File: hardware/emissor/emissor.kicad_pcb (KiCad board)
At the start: 2 copper layers, 100 x 76 mm, 49 parts, among them J1 I2C, J2 USB-C, J3 5V EXT, J4 BOIAS, SW1 RESET, SW2 BOOT, U1 ESP32-C3-MINI-1-H4X, U2 E220-900T30D, U4 USBLC6-2SC6, U5 AP2112K-3.3

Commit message: feat(hw): layout compacto de 86x52 mm nas duas placas
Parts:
- removed H3, H4: MountingHole_3.2mm_M3, MountingHole:MountingHole_3.2mm_M3
- moved R11 73.0 mm to (80.2, 27.8)
- moved F1 51.6 mm to (75.6, 28.2)
- moved J2 48.7 mm to (14.0, 47.8), turned to 0 degrees
- moved H2 46.5 mm to (82.5, 48.5)
- moved H1 44.5 mm to (3.50, 48.5)
- moved D3 41.4 mm to (68.9, 28.8)
- moved R12 38.3 mm to (45.5, 37.7)
- moved R16 37.3 mm to (61.4, 37.7)
- moved R15 37.1 mm to (57.6, 37.7)
- moved D6 37.0 mm to (53.6, 37.9)
- moved D5 36.8 mm to (49.5, 37.9)
- moved R6 34.0 mm to (30.6, 4.12)
- moved R5 33.9 mm to (26.7, 4.12)
- moved R4 33.8 mm to (22.9, 4.12)
- moved R3 33.6 mm to (19.0, 4.12)
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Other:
- board size 100 x 76 mm -> 86 x 52 mm
- board text added: "ABERTO=RESERV."
- board text added: "EMISSOR"
- board text added: "ENTRADA 5V APENAS"
- board text added: "J3: 5V+ | GND"
- board text added: "J4: BOIA-B|GND|BOIA-A|GND"
- board text added: "JP1 PAPEL:"
- board text added: "NAO LIGAR 12V"
- board text added: "NAO LIGAR O E220"
- board text added: "SEM ANTENA!"
- board text removed: "BOIAS: BAIXA | GND | ALTA | GND"
- board text removed: "EMISSOR (RESERVATORIO)"
- board text removed: "ENTRADA 5V APENAS - NAO LIGAR 12V"
- board text removed: "JP1 PAPEL: ABERTO=RESERV."
- board text removed: "NAO LIGAR O E220 SEM ANTENA!"
- board text removed: "O E220 TRANSMITE NO BOOT"

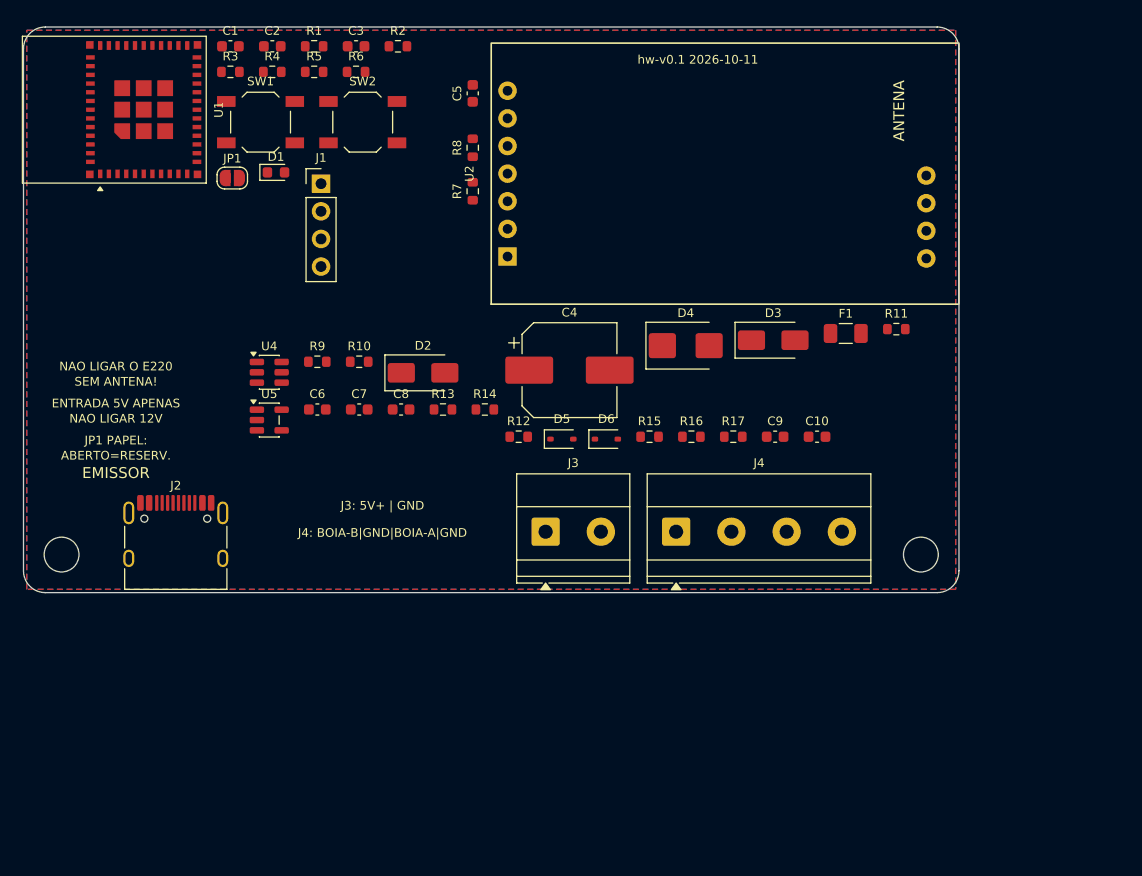
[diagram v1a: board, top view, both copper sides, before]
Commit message: wip(hw): roteador proprio, layout v2 com pecas sob o E220 (checkpoint antes de trocar para jack 12 V)
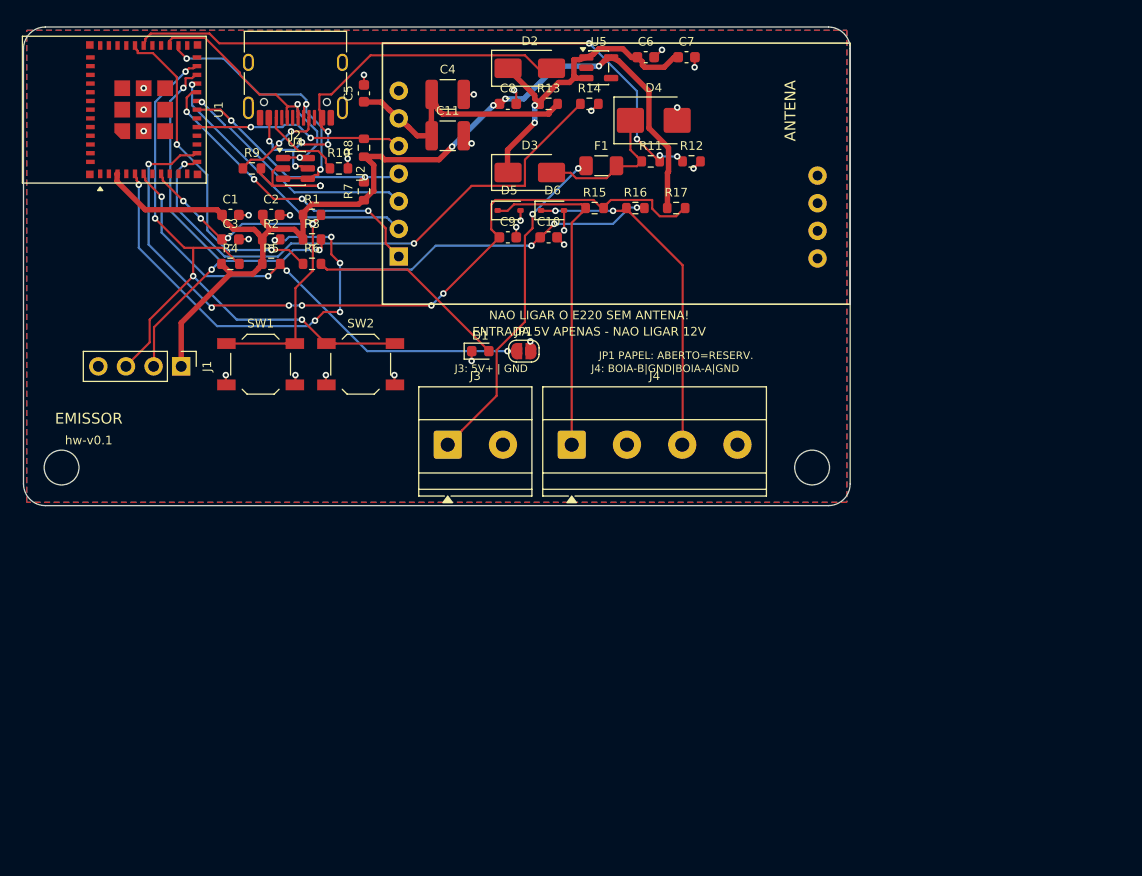
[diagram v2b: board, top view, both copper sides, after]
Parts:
- added C11: 47uF/10V, Capacitor_SMD:C_1210_3225Metric, F.Cu at (39.0, 10.0)
- C4: value 470uF/10V -> 47uF/10V; footprint Capacitor_SMD:CP_Elec_8x10.5 -> Capacitor_SMD:C_1210_3225Metric
- moved J2 44.9 mm to (25.0, 4.30), turned to 180 degrees
- moved U5 44.3 mm to (52.9, 3.75)
- moved C6 44.3 mm to (57.2, 2.77)
- moved C7 44.2 mm to (61.0, 2.77)
- moved JP1 31.2 mm to (46.0, 29.8)
- moved C10 30.7 mm to (48.3, 19.3)
- moved C9 30.7 mm to (44.5, 19.3)
- moved R12 29.9 mm to (61.4, 12.4)
- moved C8 29.8 mm to (44.5, 7.07)
- moved R13 29.7 mm to (48.3, 7.07)
- moved R14 29.7 mm to (52.0, 7.07)
- moved D2 29.7 mm to (46.5, 3.79)
- moved C4 27.7 mm to (39.0, 6.20)
- moved R11 27.3 mm to (57.7, 12.4)
- moved F1 27.3 mm to (53.1, 12.8)
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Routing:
- net +3V3: track 0.00 -> 96.5 mm, vias 0 -> 4
- net FLOAT_LOW: track 0.00 -> 73.1 mm, vias 0 -> 6
- net FLOAT_HIGH: track 0.00 -> 72.5 mm, vias 0 -> 9
- net I2C_SCL: track 0.00 -> 60.0 mm, vias 0 -> 4
- net EXT_PRESENT: track 0.00 -> 58.6 mm, vias 0 -> 4
- net BAT_ADC: track 0.00 -> 51.8 mm, vias 0 -> 2
- net ROLE_STRAP: track 0.00 -> 44.3 mm, vias 0 -> 4
- net I2C_SDA: track 0.00 -> 43.3 mm, vias 0 -> 3
- net /Alimentacao/VBUS: track 0.00 -> 40.1 mm, vias 0 -> 5
- net /MCU/MCU_EN: track 0.00 -> 36.5 mm, vias 0 -> 4
- net GND: track 0.00 -> 35.8 mm, vias 0 -> 28
- net /Entradas e Saidas/FLOAT_HIGH_IN: track 0.00 -> 31.9 mm, vias 0 -> 2
- net /Alimentacao/5V_IN: track 0.00 -> 31.2 mm, vias 0 -> 2
- net /Entradas e Saidas/FLOAT_LOW_IN: track 0.00 -> 30.8 mm
- net +5V: track 0.00 -> 30.7 mm, vias 0 -> 2
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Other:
- board size 86 x 52 mm -> 76 x 44 mm
- board text added: "ENTRADA 5V APENAS - NAO LIGAR 12V"
- board text added: "JP1 PAPEL: ABERTO=RESERV."
- board text added: "NAO LIGAR O E220 SEM ANTENA!"
- board text added: "hw-v0.1"
- board text removed: "ABERTO=RESERV."
- board text removed: "ENTRADA 5V APENAS"
- board text removed: "JP1 PAPEL:"
- board text removed: "NAO LIGAR 12V"
- board text removed: "NAO LIGAR O E220"
- board text removed: "SEM ANTENA!"
- board text removed: "hw-v0.1 2026-10-11"

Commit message: feat(hw): jack 12 V com buck AP63205, roteador proprio e serigrafia padronizada (receptor roteado; emissor com 1 net aberta)
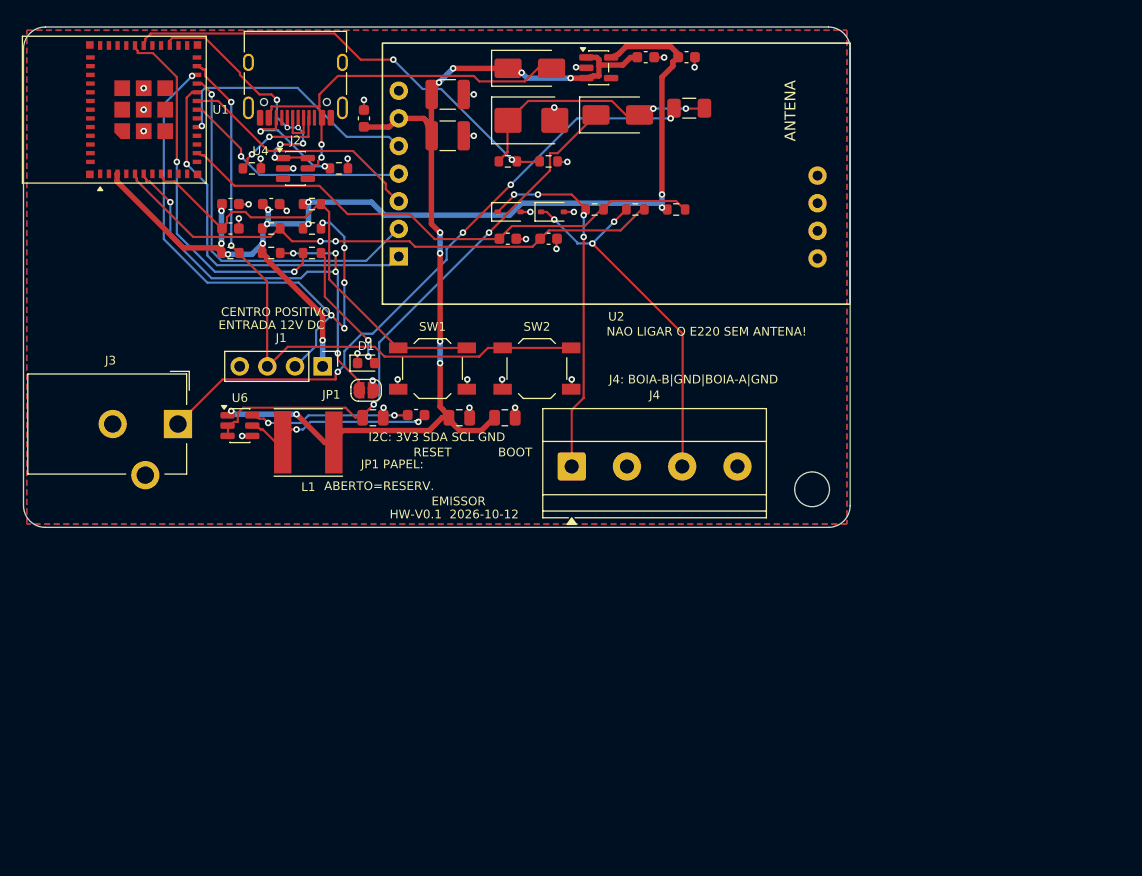
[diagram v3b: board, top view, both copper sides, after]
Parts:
- removed H2: MountingHole_3.2mm_M3, MountingHole:MountingHole_3.2mm_M3
- removed R13: 0R, Resistor_SMD:R_0603_1608Metric
- removed R14: 100k, Resistor_SMD:R_0603_1608Metric
- removed R7, R8: 10k, Resistor_SMD:R_0603_1608Metric
- added C12: 22uF/10V, Capacitor_SMD:C_0805_2012Metric, F.Cu at (40.1, 35.9)
- added C13: 22uF/10V, Capacitor_SMD:C_0805_2012Metric, F.Cu at (44.3, 35.9)
- added C14: 100nF, Capacitor_SMD:C_0603_1608Metric, F.Cu at (36.1, 35.7)
- added L1: 4.7uH, Inductor_SMD:L_Taiyo-Yuden_NR-60xx, F.Cu at (26.2, 38.2)
- added U6: AP63205WU, Package_TO_SOT_SMD:TSOT-23-6, F.Cu at (19.9, 36.6)
- C6: value 10uF -> 10uF/25V; footprint Capacitor_SMD:C_0603_1608Metric -> Capacitor_SMD:C_0805_2012Metric
- D4: value SMBJ5.0A -> SMBJ15A
- F1: value 1.5A -> 1.5A/16V
- J3: value 5V EXT -> JACK 12V; footprint TerminalBlock_Phoenix:TerminalBlock_Phoenix_MKDS-1,5-2-5.08_1x02_P5.08mm_Horizontal -> lora-pump:BarrelJack_CUI_PJ-102AH_Horizontal
- R12: value 100k -> 33k
- moved H1 69.0 mm to (72.5, 42.5)
- moved C6 41.6 mm to (32.1, 35.9)
- moved J3 24.9 mm to (14.2, 36.5), turned to -90 degrees
- moved C8 17.0 mm to (61.0, 2.77)
- moved SW2 16.2 mm to (47.2, 31.4)
- moved SW1 15.8 mm to (37.6, 31.4)
- moved JP1 14.9 mm to (31.5, 33.4)
- moved R11 13.1 mm to (44.5, 12.4)
- moved R12 13.1 mm to (48.3, 12.4)
- moved J1 13.0 mm to (27.5, 31.2)
- moved D4 11.2 mm to (46.7, 8.59)
- moved D1 10.6 mm to (31.5, 30.9)
- moved D3 9.67 mm to (54.6, 8.09)
- moved F1 9.67 mm to (61.2, 7.46)
- moved C7 3.75 mm to (57.2, 2.77)
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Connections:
- net /Alimentacao/+5V_EXT renamed /Alimentacao/+12V_F
- net /Alimentacao/5V_IN renamed /Alimentacao/12V_IN
- C11 pad 1: VCC_RF -> +5V
- C4 pad 1: VCC_RF -> +5V
- C5 pad 1: VCC_RF -> +5V
- C6 pad 1: +5V -> +12V
- D3 pad 1: +5V -> +12V
- U1 pad 12: BAT_ADC -> unconnected-(U1-IO0-Pad12)
- U2 pad 6: VCC_RF -> +5V
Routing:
- net +5V: track 30.7 -> 89.7 mm, vias 2 -> 10
- net +12V: track 0.00 -> 52.0 mm, vias 0 -> 2
- net BAT_ADC: track 51.8 -> 0.00 mm, vias 2 -> 0
- net /Alimentacao/12V_IN: track 31.2 -> 59.6 mm, vias 2 -> 4
- net VCC_RF: track 24.5 -> 0.00 mm
- net FLOAT_LOW: track 73.1 -> 50.0 mm, vias 6 -> 0
- net USB_DM: track 26.5 -> 3.80 mm, vias 3 -> 0
- net FLOAT_HIGH: track 72.5 -> 52.0 mm, vias 9 -> 2
- net /Alimentacao/SW_BUCK: track 0.00 -> 17.7 mm, vias 0 -> 2
- net EXT_PRESENT: track 58.6 -> 42.1 mm, vias 4 -> 2
- net /Alimentacao/BST: track 0.00 -> 14.8 mm, vias 0 -> 2
- net I2C_SDA: track 43.3 -> 54.2 mm, vias 3 -> 6
- net GND: track 35.8 -> 25.4 mm, vias 28 -> 31
- net /Alimentacao/+12V_F: track 13.6 -> 23.6 mm, vias 0 -> 2
- net E220_M1: track 26.2 -> 35.0 mm
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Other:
- board size 76 x 44 mm -> 76 x 46 mm
- board text added: "ABERTO=RESERV."
- board text added: "BOOT"
- board text added: "CENTRO POSITIVO"
- board text added: "ENTRADA 12V DC"
- board text added: "HW-V0.1 2026-10-12"
- board text added: "I2C: 3V3 SDA SCL GND"
- board text added: "JP1 PAPEL:"
- board text added: "RESET"
- board text removed: "ENTRADA 5V APENAS - NAO LIGAR 12V"
- board text removed: "J3: 5V+ | GND"
- board text removed: "JP1 PAPEL: ABERTO=RESERV."
- board text removed: "hw-v0.1"
